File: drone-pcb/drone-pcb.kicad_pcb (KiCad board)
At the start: 2 copper layers, 50 x 50 mm, 13 parts, among them Q1 NMOS, Q2 NPN, Q3 NPN, U1 XIAO ESP32C3

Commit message: draft pcb layout
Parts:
- added C2: 0.1u, Capacitor_SMD:C_0805_2012Metric, F.Cu at (238.2, 48.2)
- added C3: 0.1u, Capacitor_SMD:C_0805_2012Metric, F.Cu at (244.6, 48.2)
- added C4: 0.1u, Capacitor_SMD:C_0805_2012Metric, F.Cu at (252.2, 48.2)
- added D3: 1N5819, Diode_SMD:D_0805_2012Metric, F.Cu at (244.6, 45.6)
- added D4: 1N5819, Diode_SMD:D_0805_2012Metric, F.Cu at (252.2, 45.6)
- added D5: LXZ1-PL02, Diode_SMD:D_0805_2012Metric, F.Cu at (229.6, 80.2)
- added J1: Conn_02x01, Connector_PinSocket_1.27mm:PinSocket_2x01_P1.27mm_Vertical, F.Cu at (231.2, 43.1)
- added J2: Conn_02x01, Connector_PinSocket_1.27mm:PinSocket_2x01_P1.27mm_Vertical, F.Cu at (238.8, 43.1)
- added J3: Conn_02x01, Connector_PinSocket_1.27mm:PinSocket_2x01_P1.27mm_Vertical, F.Cu at (245.2, 43.1)
- added J4: Conn_02x01, Connector_PinSocket_1.27mm:PinSocket_2x01_P1.27mm_Vertical, F.Cu at (252.8, 43.1)
- added Q4: NMOS, Package_TO_SOT_SMD:TO-252-2, F.Cu at (252.2, 59.0)
- added Q5: NPN, Package_TO_SOT_SMD:SOT-23, F.Cu at (233.4, 80.2)
- added Q6: NPN, Package_TO_SOT_SMD:SOT-23, F.Cu at (237.2, 78.9)
- added R10: 39k, Resistor_SMD:R_0805_2012Metric, F.Cu at (241.0, 77.0)
- added R11: 10k, Resistor_SMD:R_0805_2012Metric, F.Cu at (241.0, 80.8)
- added R12: 10k, Resistor_SMD:R_0805_2012Metric, F.Cu at (243.6, 77.0)
- added R7: 10k, Resistor_SMD:R_0805_2012Metric, F.Cu at (244.9, 67.5)
- added R8: 10k, Resistor_SMD:R_0805_2012Metric, F.Cu at (252.5, 67.5)
- added R9: 100, Resistor_SMD:R_0805_2012Metric, F.Cu at (227.1, 80.2)
- D2: value LXZ1-PL02 -> 1N5819
- Q2, Q3: value NPN -> NMOS
- R2, R4: value 10k -> 100
- R3: value 39k -> 100
- R6: value 100 -> 10k
- U1: value XIAO ESP32C3 -> XIAO-MG24-DIP; footprint libraries:xiao_esp32c3 -> libraries:XIAO-MG24-DIP
- moved D2 42.0 mm to (238.2, 45.6), turned to 0 degrees
- moved R4 41.1 mm to (252.5, 64.9), turned to 180 degrees
- moved C1 39.6 mm to (230.6, 48.2), turned to 180 degrees
- moved D1 37.8 mm to (230.6, 45.6), turned to 0 degrees
- moved R3 36.4 mm to (244.9, 64.9), turned to 180 degrees
- moved Q1 35.0 mm to (229.5, 59.0), turned to -90 degrees
- moved Q2 34.2 mm to (237.0, 59.0), turned to -90 degrees
- moved Q3 33.7 mm to (244.6, 59.0), turned to -90 degrees
- moved R2 31.7 mm to (237.2, 65.0), turned to 180 degrees
- moved R1 27.0 mm to (229.5, 65.0), turned to 180 degrees
- moved R6 20.4 mm to (237.2, 67.2), turned to 0 degrees
- moved R5 15.9 mm to (229.5, 67.2), turned to 0 degrees
- turned U1 to 90 degrees
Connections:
- net V_MOT+ renamed V_MOT1-
- net xiao_sense_G1 renamed Motor_1
- D2 pad 1: Net-(D2-K) -> V_BAT
- D2 pad 2: Net-(D2-A) -> V_MOT2-
- Q2 pad 1: Net-(Q2-C) -> V_MOT2-
- Q2 pad 2: Net-(Q2-B) -> Net-(Q2-G)
- Q3 pad 1: Net-(D2-K) -> V_MOT3-
- Q3 pad 2: Net-(Q2-C) -> Net-(Q3-G)
- R2 pad 1: Net-(Q1-G) -> Motor_2
- R2 pad 2: 0 -> Net-(Q2-G)
- R3 pad 1: V_BAT -> Motor_3
- R3 pad 2: Net-(Q2-B) -> Net-(Q3-G)
- R4 pad 1: Net-(Q2-B) -> Motor_4
- R4 pad 2: 0 -> Net-(Q4-G)
- R5 pad 1: V_BAT -> Net-(Q1-G)
- R5 pad 2: Net-(Q2-C) -> 0
- R6 pad 1: V_BAT -> Net-(Q2-G)
- R6 pad 2: Net-(D2-A) -> 0
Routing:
- net V_BAT: track 0.00 -> 49.8 mm
- net Net-(Q5-B): track 0.00 -> 9.89 mm
- net Net-(Q4-G): track 0.00 -> 7.87 mm
- net Net-(Q3-G): track 0.00 -> 7.87 mm
- net Net-(Q1-G): track 0.00 -> 7.81 mm
- net Net-(Q2-G): track 0.00 -> 7.64 mm
- net Net-(Q6-B): track 0.00 -> 6.19 mm
- net Net-(D5-A): track 0.00 -> 3.34 mm
- net Net-(D5-K): track 0.00 -> 2.88 mm
- net 0: track 0.00 -> 2.46 mm
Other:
- board size 50 x 50 mm -> 25 x 50 mm

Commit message: apdejt
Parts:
- added C5: 0.1u, Capacitor_SMD:C_0603_1608Metric, F.Cu at (215.0, 70.6)
- added C6: 470u, Capacitor_SMD:C_0603_1608Metric, F.Cu at (196.6, 81.7)
- added J5: Conn_02x01, jst:JST_PH_S2B-PH-SM4-TB_1x02-1MP_P2.00mm_Horizontal_footprint, F.Cu at (178.3, 71.5)
- added R13: 470k, Resistor_SMD:R_0603_1608Metric, F.Cu at (215.0, 72.4)
- added R14: 470k, Resistor_SMD:R_0603_1608Metric, F.Cu at (215.0, 69.0)
- C1, C2, C3, C4: footprint Capacitor_SMD:C_0805_2012Metric -> Capacitor_SMD:C_0603_1608Metric
- J1, J2, J3, J4: footprint Connector_PinSocket_1.27mm:PinSocket_2x01_P1.27mm_Vertical -> jst:JST_PH_S2B-PH-SM4-TB_1x02-1MP_P2.00mm_Horizontal_footprint
- Q1, Q2, Q3, Q4: footprint Package_TO_SOT_SMD:TO-252-2 -> Package_TO_SOT_SMD:SOT-23
- R1, R10, R11, R12, R2, R3, R4, R5, R6, R7, R8, R9: footprint Resistor_SMD:R_0805_2012Metric -> Resistor_SMD:R_0603_1608Metric
- moved J3 76.8 mm to (178.3, 80.9), turned to -90 degrees
- moved R10 69.3 mm to (274.7, 16.4)
- moved R11 69.3 mm to (274.7, 20.2)
- moved R12 69.3 mm to (277.2, 16.4)
- moved R9 69.3 mm to (260.7, 19.6)
- moved Q6 69.3 mm to (270.9, 18.3)
- moved D5 69.3 mm to (263.3, 19.6)
- moved Q5 69.3 mm to (267.1, 19.6)
- moved D3 68.0 mm to (185.8, 79.9), turned to 180 degrees
- moved C3 65.9 mm to (185.8, 78.1), turned to 0 degrees
- moved Q3 63.7 mm to (185.5, 82.6), turned to 180 degrees
- moved R3 58.7 mm to (189.2, 83.5)
- moved R7 57.5 mm to (189.2, 81.7), turned to 180 degrees
- moved J1 56.2 mm to (178.3, 62.1), turned to -90 degrees
- moved D4 48.5 mm to (220.0, 81.9)
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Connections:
- Q1 pad 1: V_MOT1- -> Net-(Q1-G)
- Q1 pad 2: Net-(Q1-G) -> GND
- Q1 pad 3: 0 -> V_MOT1-
- Q2 pad 1: V_MOT2- -> Net-(Q2-D)
- Q2 pad 2: Net-(Q2-G) -> GND
- Q2 pad 3: 0 -> V_MOT2-
- Q3 pad 1: V_MOT3- -> Net-(Q3-D)
- Q3 pad 2: Net-(Q3-G) -> GND
- Q3 pad 3: 0 -> V_MOT3-
- Q4 pad 1: V_MOT4- -> Net-(Q4-D)
- Q4 pad 2: Net-(Q4-G) -> GND
- Q4 pad 3: 0 -> V_MOT4-
- R2 pad 2: Net-(Q2-G) -> Net-(Q2-D)
- R3 pad 2: Net-(Q3-G) -> Net-(Q3-D)
- R4 pad 2: Net-(Q4-G) -> Net-(Q4-D)
- R5 pad 2: 0 -> GND
- R6 pad 1: Net-(Q2-G) -> Net-(Q2-D)
- R6 pad 2: 0 -> GND
- R7 pad 1: Net-(Q3-G) -> Net-(Q3-D)
- R7 pad 2: 0 -> GND
- R8 pad 1: Net-(Q4-G) -> Net-(Q4-D)
- R8 pad 2: 0 -> GND
- U1 pad 1: unconnected-(U1-PC00_A0_D0-Pad1) -> Motor_1
- U1 pad 10: unconnected-(U1-PA04_A9_D9_MISO-Pad10) -> Motor_4
- U1 pad 11: unconnected-(U1-PA05_A10_D10_MOSI-Pad11) -> Motor_2
- U1 pad 13: unconnected-(U1-GND-Pad13) -> GND
- U1 pad 2: unconnected-(U1-PC01_A1_D1-Pad2) -> Motor_3
- U1 pad 8: unconnected-(U1-PC07_A7_D7_RX-Pad8) -> Net-(U1-PC07_A7_D7_RX)
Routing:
- net V_BAT: track 49.8 -> 36.3 mm
- net Net-(U1-PC07_A7_D7_RX): track 0.00 -> 8.78 mm
- net V_MOT1-: track 0.00 -> 8.51 mm
- net V_MOT4-: track 0.00 -> 8.50 mm
- net V_MOT2-: track 0.00 -> 8.50 mm
- net V_MOT3-: track 0.00 -> 8.50 mm
- net Net-(Q4-G): track 7.87 -> 0.00 mm
- net Net-(Q3-G): track 7.87 -> 0.00 mm
- net GND: track 0.00 -> 7.69 mm
- net Net-(Q2-G): track 7.64 -> 0.00 mm
- net Net-(Q2-D): track 0.00 -> 4.43 mm
- net Net-(Q3-D): track 0.00 -> 4.43 mm
- net Net-(Q4-D): track 0.00 -> 4.36 mm
- net Net-(Q1-G): track 7.81 -> 4.43 mm
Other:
- board size 25 x 50 mm -> 60 x 27.5 mm

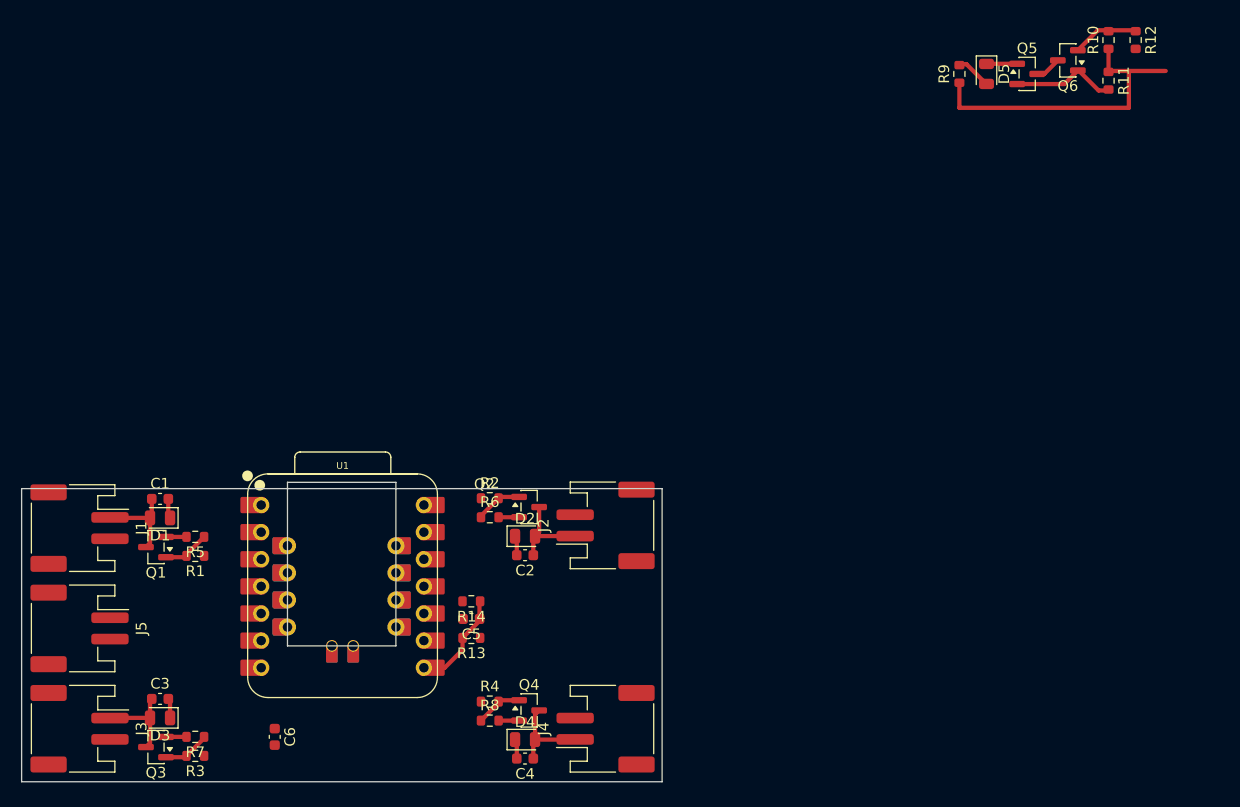
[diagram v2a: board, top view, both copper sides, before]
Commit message: pcb design, ground, vcc to be changed yet
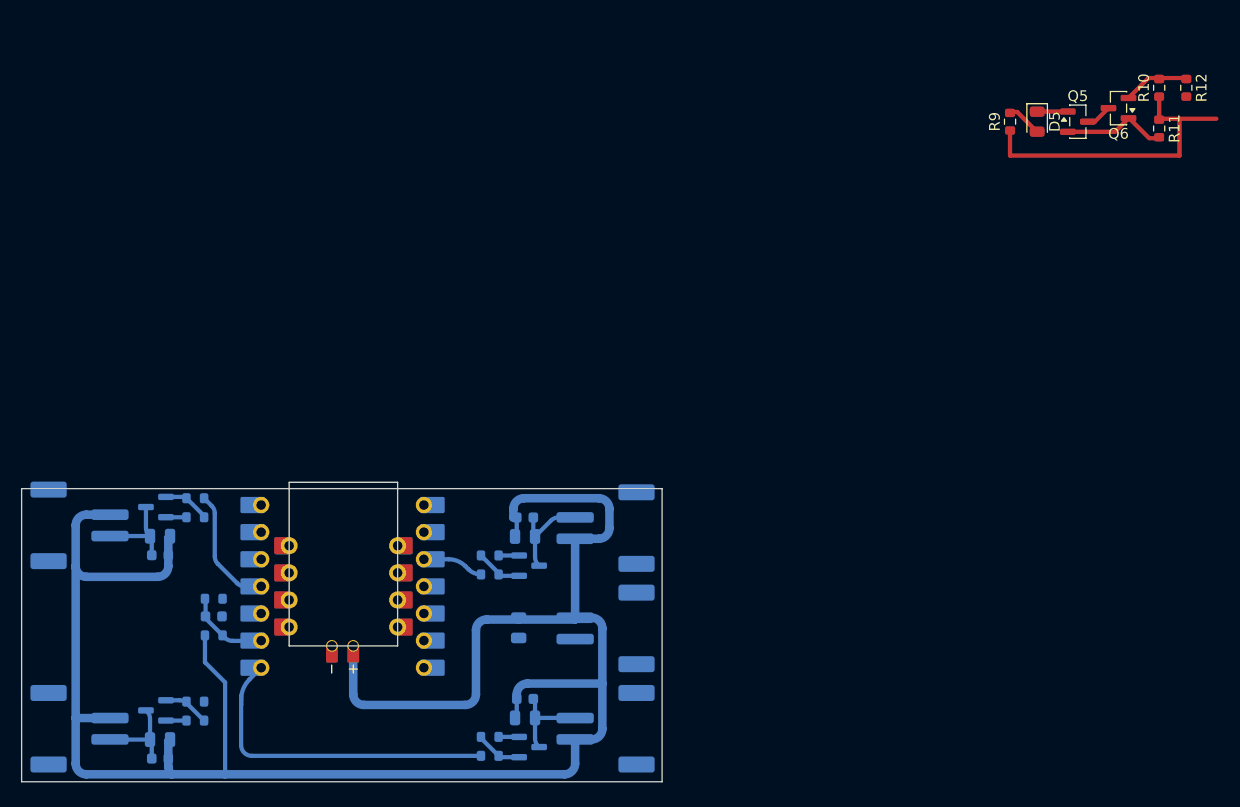
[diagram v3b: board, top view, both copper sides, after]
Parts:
- C1, C2, C3, C4, C5, D1, D2, D3, D4, Q1, Q2, Q3, Q4, R1, R13, R14, R2, R3, R4, R5, R6, R7, R8, U1: moved to B.Cu
- C6: footprint Capacitor_SMD:C_0603_1608Metric -> Capacitor_SMD:C_0805_2012Metric; moved to B.Cu
- J1, J2, J3, J4, J5: footprint jst:JST_PH_S2B-PH-SM4-TB_1x02-1MP_P2.00mm_Horizontal_footprint -> Connector_JST:JST_PH_S2B-PH-SM4-TB_1x02-1MP_P2.00mm_Horizontal; moved to B.Cu
- moved J1 49.3 mm to (227.6, 62.1)
- moved J2 49.3 mm to (178.3, 61.9)
- moved J3 49.3 mm to (227.6, 80.9)
- moved J4 49.3 mm to (178.3, 80.9)
- moved J5 49.3 mm to (227.6, 71.5)
- moved Q1 35.0 mm to (220.4, 65.7), turned to 0 degrees
- moved Q2 35.0 mm to (185.5, 60.2), turned to 180 degrees
- moved Q3 35.0 mm to (220.4, 82.6), turned to 0 degrees
- moved Q4 35.0 mm to (185.5, 79.2), turned to 180 degrees
- moved C1 34.2 mm to (220.0, 61.1), turned to 180 degrees
- moved D1 34.2 mm to (220.0, 62.9), turned to 0 degrees
- moved C2 34.2 mm to (185.8, 64.7), turned to 0 degrees
- moved C3 34.2 mm to (220.0, 78.1), turned to 180 degrees
- moved C4 34.2 mm to (185.8, 83.7), turned to 0 degrees
- moved D2 34.2 mm to (185.8, 62.9), turned to 180 degrees
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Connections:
- C5 pad 1: Net-(U1-PC07_A7_D7_RX) -> Net-(U1-PA03_A8_D8_SCK)
- R13 pad 2: Net-(U1-PC07_A7_D7_RX) -> Net-(U1-PA03_A8_D8_SCK)
- R14 pad 1: Net-(U1-PC07_A7_D7_RX) -> Net-(U1-PA03_A8_D8_SCK)
- U1 pad 1: Motor_1 -> unconnected-(U1-PC00_A0_D0-Pad1)
- U1 pad 2: Motor_3 -> unconnected-(U1-PC01_A1_D1-Pad2)
- U1 pad 3: unconnected-(U1-PC02_A2_D2-Pad3) -> Motor_1
- U1 pad 8: Net-(U1-PC07_A7_D7_RX) -> Motor_3
- U1 pad 9: unconnected-(U1-PA03_A8_D8_SCK-Pad9) -> Net-(U1-PA03_A8_D8_SCK)
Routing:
- net V_BAT: track 36.3 -> 223.1 mm
- net Motor_3: track 0.00 -> 31.7 mm
- net Motor_2: track 0.00 -> 10.7 mm
- net Net-(U1-PC07_A7_D7_RX): track 8.78 -> 0.00 mm
- net Net-(U1-PA03_A8_D8_SCK): track 0.00 -> 7.13 mm
- net Motor_1: track 0.00 -> 4.97 mm
- net unconnected-(U1-PC00_A0_D0-Pad1): track 0.00 -> 1.08 mm
- net V_MOT1-: track 8.51 -> 9.20 mm

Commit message: apdejt rev 2
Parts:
- removed C1, C2, C3, C4: 0.1u, Capacitor_SMD:C_0603_1608Metric
- removed D5: LXZ1-PL02, Diode_SMD:D_0805_2012Metric
- removed Q5, Q6: NPN, Package_TO_SOT_SMD:SOT-23
- removed R10: 39k, Resistor_SMD:R_0603_1608Metric
- removed R11, R12: 10k, Resistor_SMD:R_0603_1608Metric
- removed R9: 100, Resistor_SMD:R_0603_1608Metric
- C5, C6, R1, R13, R14, R2, R4, R5, R6, R8: moved to F.Cu
- D1, D2, D3, D4: value 1N5819 -> SD1206T040S2R0; footprint Diode_SMD:D_0805_2012Metric -> Diode_SMD:D_1206_3216Metric; moved to F.Cu
- J1: value Conn_02x01 -> MOT_1; footprint Connector_JST:JST_PH_S2B-PH-SM4-TB_1x02-1MP_P2.00mm_Horizontal -> Connector_Wire:SolderWire-0.1sqmm_1x02_P3.6mm_D0.4mm_OD1mm; moved to F.Cu
- J2: value Conn_02x01 -> MOT_2; footprint Connector_JST:JST_PH_S2B-PH-SM4-TB_1x02-1MP_P2.00mm_Horizontal -> Connector_Wire:SolderWire-0.1sqmm_1x02_P3.6mm_D0.4mm_OD1mm; moved to F.Cu
- J3: value Conn_02x01 -> MOT_3; footprint Connector_JST:JST_PH_S2B-PH-SM4-TB_1x02-1MP_P2.00mm_Horizontal -> Connector_Wire:SolderWire-0.1sqmm_1x02_P3.6mm_D0.4mm_OD1mm; moved to F.Cu
- J4: value Conn_02x01 -> MOT_4; footprint Connector_JST:JST_PH_S2B-PH-SM4-TB_1x02-1MP_P2.00mm_Horizontal -> Connector_Wire:SolderWire-0.1sqmm_1x02_P3.6mm_D0.4mm_OD1mm; moved to F.Cu
- J5: value Conn_02x01 -> BAT; footprint Connector_JST:JST_PH_S2B-PH-SM4-TB_1x02-1MP_P2.00mm_Horizontal -> Connector_Wire:SolderWire-0.1sqmm_1x02_P3.6mm_D0.4mm_OD1mm; moved to F.Cu
- Q1, Q2, Q3, Q4: value NMOS -> AO3400A; moved to F.Cu
- R3: value 100 -> 10k; moved to F.Cu
- R7: value 10k -> 100; moved to F.Cu
- U1: value XIAO-MG24-DIP -> XIAO ESP32C3; moved to F.Cu
- moved J1 136.2 mm to (94.5, 91.0), turned to -45 degrees
- moved D1 130.8 mm to (93.2, 94.9), turned to 135 degrees
- moved Q1 125.4 mm to (97.1, 88.5), turned to -135 degrees
- moved R1 118.9 mm to (98.8, 82.2), turned to 180 degrees
- moved R5 118.9 mm to (98.8, 80.4), turned to 180 degrees
- moved J5 111.5 mm to (117.9, 91.7), turned to 180 degrees
- moved D4 97.4 mm to (93.9, 49.8), turned to -135 degrees
- moved J3 94.1 mm to (137.7, 52.9), turned to 135 degrees
- moved Q4 90.7 mm to (97.7, 56.2), turned to 135 degrees
- moved Q3 89.5 mm to (135.1, 55.5), turned to 45 degrees
- moved J4 87.5 mm to (95.2, 53.7), turned to 45 degrees
- moved U1 87.0 mm to (116.1, 62.2)
- moved D3 86.7 mm to (139.0, 49.1), turned to -45 degrees
- moved Q2 57.8 mm to (135.1, 88.5), turned to -45 degrees
- moved D2 56.7 mm to (139.0, 94.9), turned to 45 degrees
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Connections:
- net V_MOT1- renamed Net-(D1-A)
- net V_MOT2- renamed Net-(D2-A)
- net V_MOT3- renamed Net-(D3-A)
- net V_MOT4- renamed Net-(D4-A)
- C5 pad 1: Net-(U1-PA03_A8_D8_SCK) -> BAT_SENS
- J5 pad 1: V_BAT -> GND
- J5 pad 2: GND -> V_BAT
- R1 pad 1: Motor_1 -> MOT_1
- R13 pad 2: Net-(U1-PA03_A8_D8_SCK) -> BAT_SENS
- R14 pad 1: Net-(U1-PA03_A8_D8_SCK) -> BAT_SENS
- R2 pad 1: Motor_2 -> MOT_2
- R3 pad 1: Motor_3 -> MOT_2
- R3 pad 2: Net-(Q3-G) -> GND
- R4 pad 1: Motor_4 -> MOT_3
- R4 pad 2: Net-(Q4-G) -> Net-(Q3-G)
- R5 pad 1: Net-(Q1-G) -> MOT_1
- R6 pad 1: Net-(Q2-G) -> MOT_3
- R7 pad 1: Net-(Q3-G) -> MOT_4
- R7 pad 2: GND -> Net-(Q4-G)
- R8 pad 1: Net-(Q4-G) -> MOT_4
- U1 pad 10: Motor_4 -> unconnected-(U1-D9-Pad10)
- U1 pad 11: Motor_2 -> unconnected-(U1-D10-Pad11)
- U1 pad 13: GND -> unconnected-(U1-GND-Pad13)
- U1 pad 3: Motor_1 -> unconnected-(U1-D2-Pad3)
- U1 pad 8: Motor_3 -> unconnected-(U1-D7-Pad8)
- U1 pad 9: Net-(U1-PA03_A8_D8_SCK) -> unconnected-(U1-D8-Pad9)
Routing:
- net V_BAT: track 223.1 -> 106.4 mm
- net GND: track 7.69 -> 40.8 mm
- net Motor_3: track 31.7 -> 0.00 mm
- net Motor_2: track 10.7 -> 0.00 mm
- net Net-(Q5-B): track 9.89 -> 0.00 mm
- net Net-(U1-PA03_A8_D8_SCK): track 7.13 -> 0.00 mm
- net Net-(Q6-B): track 6.19 -> 0.00 mm
- net Motor_1: track 4.97 -> 0.00 mm
- net Net-(Q3-G): track 4.43 -> 0.00 mm
- net Net-(Q1-G): track 4.43 -> 0.00 mm
- net Net-(Q2-G): track 4.43 -> 0.00 mm
- net Net-(Q4-G): track 4.31 -> 0.00 mm
- net Net-(D5-A): track 3.34 -> 0.00 mm
- net Net-(D5-K): track 2.88 -> 0.00 mm
- net Net-(D1-A): track 9.20 -> 6.45 mm
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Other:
- board size 60 x 27.5 mm -> 100 x 100 mm

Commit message: rev 2 apdejt
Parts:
- moved R8 118.2 mm to (100.1, 58.6), turned to -135 degrees
- moved R14 94.5 mm to (121.0, 78.8), turned to 0 degrees
- moved C5 94.2 mm to (121.0, 77.1), turned to 0 degrees
- moved R13 93.9 mm to (121.0, 75.3), turned to 0 degrees
- moved R7 90.0 mm to (101.3, 59.9), turned to -135 degrees
- moved R2 89.3 mm to (131.4, 85.0), turned to 45 degrees
- moved R4 87.0 mm to (131.5, 59.1), turned to 135 degrees
- moved R6 83.9 mm to (132.8, 57.8), turned to 135 degrees
- moved C6 77.6 mm to (111.0, 89.1), turned to 180 degrees
- moved R3 56.5 mm to (132.7, 86.2), turned to 45 degrees
- moved R5 5.76 mm to (99.4, 86.1), turned to -45 degrees
- moved R1 3.25 mm to (100.6, 84.9), turned to -45 degrees
- moved J4 0.11 mm to (95.3, 53.7)
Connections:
- U1 pad 1: unconnected-(U1-D0-Pad1) -> MOT_4
- U1 pad 10: unconnected-(U1-D9-Pad10) -> MOT_2
- U1 pad 11: unconnected-(U1-D10-Pad11) -> MOT_3
- U1 pad 31: (no net) -> V_BAT
- U1 pad 32: (no net) -> GND
- U1 pad 7: unconnected-(U1-D6-Pad7) -> MOT_1
- U1 pad 9: unconnected-(U1-D8-Pad9) -> BAT_SENS
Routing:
- net GND: track 40.8 -> 187.0 mm, vias 0 -> 5
- net V_BAT: track 106.4 -> 152.2 mm
- net MOT_2: track 0.00 -> 26.6 mm
- net MOT_1: track 1.78 -> 26.1 mm
- net BAT_SENS: track 0.00 -> 13.1 mm
- net MOT_3: track 0.00 -> 10.5 mm
- net MOT_4: track 0.00 -> 10.1 mm
- net Net-(Q2-G): track 0.00 -> 5.17 mm
- net Net-(Q4-G): track 0.00 -> 5.08 mm
- net Net-(Q3-G): track 0.00 -> 4.96 mm
- net Net-(Q1-G): track 0.00 -> 4.90 mm
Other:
- outline, holes or cut-outs redrawn

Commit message: uptodate_pcb_v1.0
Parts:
- C5, C6, D1, D2, D3, D4, J1, J2, J3, J4, J5, Q1, Q2, Q3, Q4, R1, R13, R14, R2, R3, R4, R5, R6, R7, R8, U1: moved to B.Cu
- moved D1 45.7 mm to (139.0, 94.9), turned to 45 degrees
- moved D2 45.7 mm to (93.2, 94.9), turned to 135 degrees
- moved D3 45.7 mm to (93.2, 49.1), turned to -135 degrees
- moved D4 44.4 mm to (138.3, 49.8), turned to -45 degrees
- moved J1 43.2 mm to (137.7, 91.0), turned to -135 degrees
- moved J3 43.2 mm to (94.5, 52.9), turned to 45 degrees
- moved J2 43.2 mm to (94.5, 91.0), turned to -45 degrees
- moved J4 41.7 mm to (137.0, 53.7), turned to 135 degrees
- moved Q1 38.0 mm to (135.1, 88.5), turned to -45 degrees
- moved Q2 38.0 mm to (97.1, 88.5), turned to -135 degrees
- moved Q3 38.0 mm to (97.1, 55.5), turned to 135 degrees
- moved Q4 36.8 mm to (134.5, 56.2), turned to 45 degrees
- moved R5 33.5 mm to (132.9, 86.1), turned to -135 degrees
- moved R6 33.3 mm to (99.5, 57.8), turned to 45 degrees
- moved R3 33.2 mm to (99.5, 86.2), turned to 135 degrees
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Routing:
- net GND: track 187.0 -> 193.4 mm
- net V_BAT: track 152.2 -> 150.7 mm
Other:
- board size 100 x 100 mm -> 55 x 55 mm
